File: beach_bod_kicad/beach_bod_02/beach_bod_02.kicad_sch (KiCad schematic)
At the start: 72 parts, among them J1 Conn_01x01, J3 BNC5-J-P-GN-RA-BH2D, J4 Conn_01x01, J5 USB4085-GF-A_REVA4, J6 USB4085-GF-A_REVA4, Q1 AO3401A, U1 LTC6269, U2 LTC6268, U3 LM7301_SOT23_5

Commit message: Routed beach_bod_02
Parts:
- C32: renamed from C34; footprint Capacitor_SMD:C_1210_3225Metric_Pad1.33x2.70mm_HandSolder -> Capacitor_SMD:C_0603_1608Metric_Pad1.08x0.95mm_HandSolder
- renumbered C2 to C1, C6 to C10, C7 to C11, C8 to C12, C9 to C13, C12 to C14, C13 to C15, C14 to C16, C16 to C17, C17 to C18, C22 to C19, C3 to C2, C23 to C20, C24 to C21, C25 to C22, C26 to C23, C27 to C24, C28 to C25, C29 to C26, C30 to C27, C31 to C28, C32 to C29, C4 to C3, C33 to C30, C10 to C31, C5 to C4, C18 to C5, C19 to C6, C20 to C7, C21 to C8, C1 to C9, J3 to J2, J4 to J3, J5 to J4, J6 to J5, R3 to R1, R18 to R10, R1 to R11, R2 to R12, R7 to R13, R9 to R14, R11 to R15, R12 to R16, R14 to R17, R19 to R18, R20 to R19, R4 to R2, R21 to R20, R22 to R21, R23 to R22, R25 to R23, R27 to R24, R28 to R25, R5 to R3, R6 to R4, R8 to R5, R13 to R6, R15 to R7, R16 to R8, R17 to R9
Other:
- moved on the sheet: C1, C2, C26, C27, C28, C29, C3, C30, C31, C32, C4, C5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

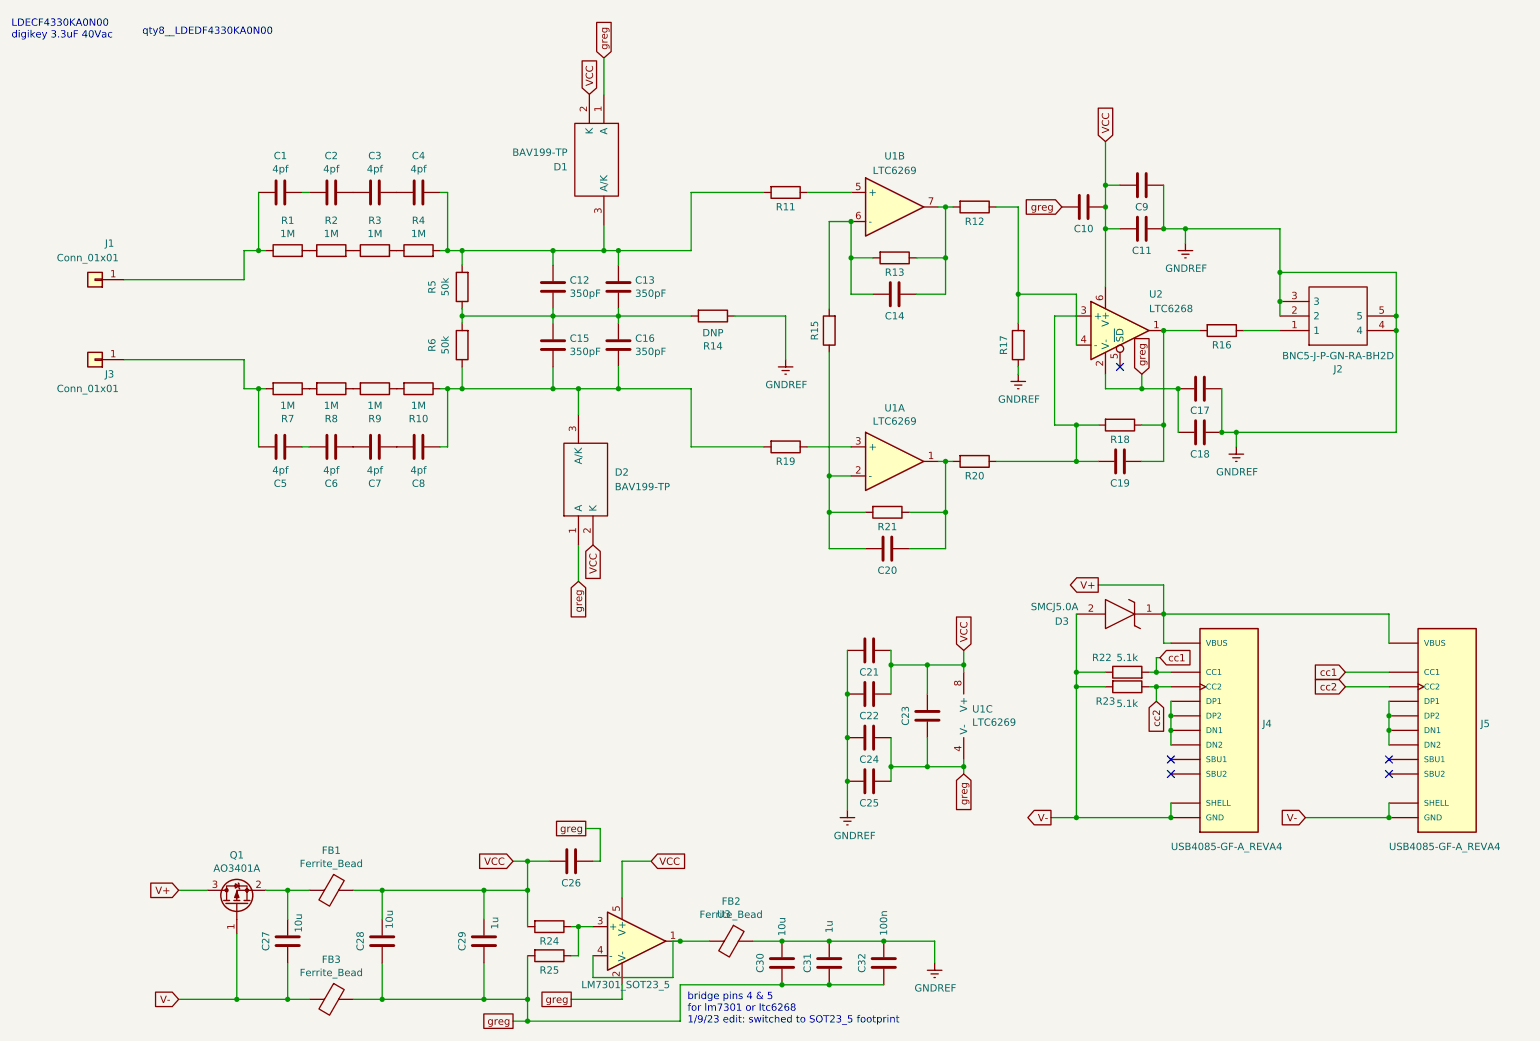
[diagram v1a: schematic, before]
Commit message: Version saving, added trimpot & BOM
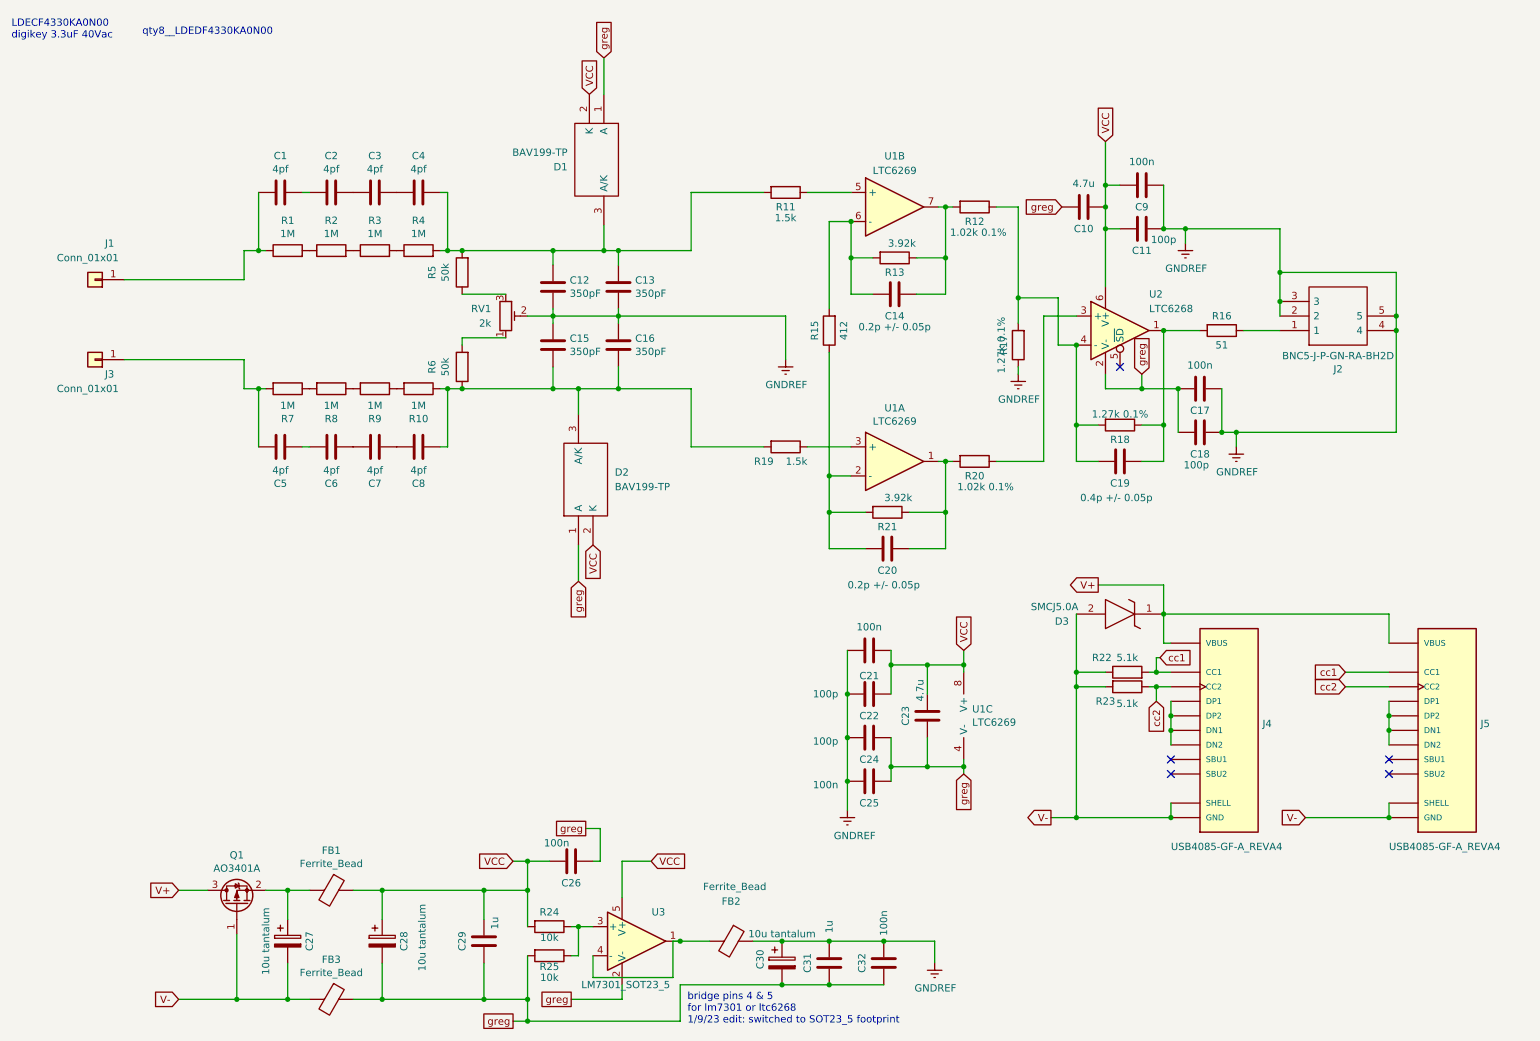
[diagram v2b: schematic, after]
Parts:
- removed R14: DNP, Resistor_SMD:R_0805_2012Metric_Pad1.20x1.40mm_HandSolder, symbol Device:R
- added RV1: 2k, Potentiometer_SMD:Potentiometer_Bourns_3314J_Vertical, symbol Device:R_Potentiometer_Trim
- C1, C12, C13, C15, C16, C2, C3, C4, C5, C6, C7, C8: footprint Capacitor_SMD:C_0805_2012Metric_Pad1.18x1.45mm_HandSolder -> Capacitor_SMD:C_0603_1608Metric_Pad1.08x0.95mm_HandSolder
- C10, C23: value ~ -> 4.7u
- C11, C18, C22, C24: value ~ -> 100p
- C14, C20: value ~ -> 0.2p +/- 0.05p
- C17, C21, C25, C26, C9: value ~ -> 100n
- C19: value ~ -> 0.4p +/- 0.05p
- C27, C28, C30: value 10u -> 10u tantalum; symbol Device:C -> Device:C_Polarized
- R1, R10, R2, R3, R4, R5, R6, R7, R8, R9: footprint Resistor_SMD:R_0805_2012Metric_Pad1.20x1.40mm_HandSolder -> Resistor_SMD:R_0603_1608Metric_Pad0.98x0.95mm_HandSolder
- R11, R19: value ~ -> 1.5k
- R12, R20: value ~ -> 1.02k 0.1%
- R13, R21: value ~ -> 3.92k
- R15: value ~ -> 412
- R16: value ~ -> 51
- R17, R18: value ~ -> 1.27k 0.1%
- R24, R25: value ~ -> 10k
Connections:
- net GNDREF: now also C12.1, C13.1, C15.2, C16.2, C30.1, RV1.2; no longer C30.2
- net V-: now also C27.2; no longer C27.1
- net VCC: now also C28.1; no longer C28.2
- net greg: now also C28.2, C30.2; no longer C28.1, C30.1
- net at FB1.2, Q1.2 (S): now also C27.1; no longer C27.2
- net at C19.2, R18.2: now also R12.1, R17.2, U2.4 (-); no longer R20.1, U2.3 (+)
- new net: R6.2, RV1.1
- new net: R5.1, RV1.3
- new net: R20.1, U2.3 (+)
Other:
- moved on the sheet: R5, R6

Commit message: Added beach_bod_v02_cart
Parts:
- C26: footprint Capacitor_SMD:C_0805_2012Metric_Pad1.18x1.45mm_HandSolder -> Capacitor_SMD:C_0603_1608Metric_Pad1.08x0.95mm_HandSolder
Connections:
- net sig_P: now reaches C12.2, C13.2, C4.1, D1.3 (A/K), R11.2, R4.2, R5.2
- net sig_N: now reaches C15.1, C16.1, C8.2, D2.3 (A/K), R10.1, R19.2, R6.1
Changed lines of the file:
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@@
   (junction (at 80.01 168.275) (diameter 0) (color 0 0 0 0)
   )
+  (junction (at 100.965 56.515) (diameter 0) (color 0 0 0 0)
+  )
   (junction (at 105.41 191.135) (diameter 0) (color 0 0 0 0)
   )
@@
   )
   (junction (at 201.295 155.575) (diameter 0) (color 0 0 0 0)
+  )
+  (junction (at 101.6 80.645) (diameter 0) (color 0 0 0 0)
   )
   (junction (at 236.855 60.325) (diameter 0) (color 0 0 0 0)
@@
     (stroke (width 0) (type default) (color 0 0 0 0))
   )
+  (wire (pts (xy 101.6 86.36) (xy 101.6 80.645))
+    (stroke (width 0) (type default) (color 0 0 0 0))
+  )
   (wire (pts (xy 93.98 64.135) (xy 101.6 64.135))
     (stroke (width 0) (type default) (color 0 0 0 0))
@@
     (stroke (width 0) (type default) (color 0 0 0 0))
   )
+  (wire (pts (xy 101.6 80.645) (xy 109.855 80.645))
+    (stroke (width 0) (type default) (color 0 0 0 0))
+  )
   (wire (pts (xy 55.88 80.645) (xy 58.42 80.645))
     (stroke (width 0) (type default) (color 0 0 0 0))
@@
     (stroke (width 0) (type default) (color 0 0 0 0))
   )
+  (wire (pts (xy 100.965 56.515) (xy 109.855 56.515))
+    (stroke (width 0) (type default) (color 0 0 0 0))
+  )
   (wire (pts (xy 161.29 149.225) (xy 161.29 141.605))
     (stroke (width 0) (type default) (color 0 0 0 0))
@@
     (stroke (width 0) (type default) (color 0 0 0 0))
   )
-  (wire (pts (xy 93.98 80.645) (xy 109.855 80.645))
+  (wire (pts (xy 93.98 80.645) (xy 101.6 80.645))
     (stroke (width 0) (type default) (color 0 0 0 0))
   )
@@
     (stroke (width 0) (type default) (color 0 0 0 0))
   )
+  (wire (pts (xy 100.965 52.705) (xy 100.965 56.515))
+    (stroke (width 0) (type default) (color 0 0 0 0))
+  )
   (wire (pts (xy 206.375 78.105) (xy 206.375 80.645))
     (stroke (width 0) (type default) (color 0 0 0 0))
@@
     (stroke (width 0) (type default) (color 0 0 0 0))
   )
-  (wire (pts (xy 93.98 56.515) (xy 109.855 56.515))
+  (wire (pts (xy 93.98 56.515) (xy 100.965 56.515))
     (stroke (width 0) (type default) (color 0 0 0 0))
   )
@@
     )
   )
+  (global_label "sig_N" (shape input) (at 101.6 86.36 0) (fields_autoplaced)
+    (effects (font (size 1.27 1.27)) (justify left))
+    (property "Intersheet References" "${INTERSHEET_REFS}" (id 0) (at 109.0042 86.2806 0)
+      (effects (font (size 1.27 1.27)) (justify left) hide)
+    )
+  )
   (global_label "greg" (shape input) (at 118.745 22.86 90) (fields_autoplaced)
     (effects (font (size 1.27 1.27)) (justify left))
@@
     (property "Intersheet References" "${INTERSHEET_REFS}" (id 0) (at 12.065 -17.145 0)
       (effects (font (size 1.27 1.27)) hide)
+    )
+  )
+  (global_label "sig_P" (shape input) (at 100.965 52.705 0) (fields_autoplaced)
+    (effects (font (size 1.27 1.27)) (justify left))
+    (property "Intersheet References" "${INTERSHEET_REFS}" (id 0) (at 108.3087 52.6256 0)
+      (effects (font (size 1.27 1.27)) (justify left) hide)
     )
   )
@@
     (property "Reference" "C26" (id 0) (at 113.03 167.005 90))
     (property "Value" "100n" (id 1) (at 110.49 160.02 90))
-    (property "Footprint" "Capacitor_SMD:C_0805_2012Metric_Pad1.18x1.45mm_HandSolder" (id 2) (at 109.22 164.1602 0)
+    (property "Footprint" "Capacitor_SMD:C_0603_1608Metric_Pad1.08x0.95mm_HandSolder" (id 2) (at 109.22 164.1602 0)
       (effects (font (size 1.27 1.27)) hide)
     )
@@
     (pin "5")
     (pin "6")
-    (pin "1")
     (pin "3")
     (pin "4")
+    (pin "1")
   )
   (symbol (lib_id "Device:R") (at 93.98 76.835 180) (unit 1)
@@
     (in_bom yes) (on_board yes)
     (property "Reference" "R17" (id 0) (at 188.595 73.025 90))
-    (property "Value" "1.27k 0.1%" (id 1) (at 188.1886 73.025 90))
+    (property "Value" "1.27k 0.1%" (id 1) (at 186.055 73.025 90))
     (property "Footprint" "Resistor_SMD:R_0805_2012Metric_Pad1.20x1.40mm_HandSolder" (id 2) (at 192.913 73.025 90)
       (effects (font (size 1.27 1.27)) hide)
@@
     )
     (path "/0bdc1f64-b4e0-4694-a05e-d977ce9c8c90"
-      (reference "C26") (unit 1) (value "100n") (footprint "Capacitor_SMD:C_0805_2012Metric_Pad1.18x1.45mm_HandSolder")
+      (reference "C26") (unit 1) (value "100n") (footprint "Capacitor_SMD:C_0603_1608Metric_Pad1.08x0.95mm_HandSolder")
     )
     (path "/f9dabf6e-b552-40fe-b1f0-5f7a78e5213a"
